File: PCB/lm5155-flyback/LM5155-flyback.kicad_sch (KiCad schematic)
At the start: 24 parts, among them Q1 Q_NMOS_DGS, T1 EP7-5801_750315825, U1 LM5155

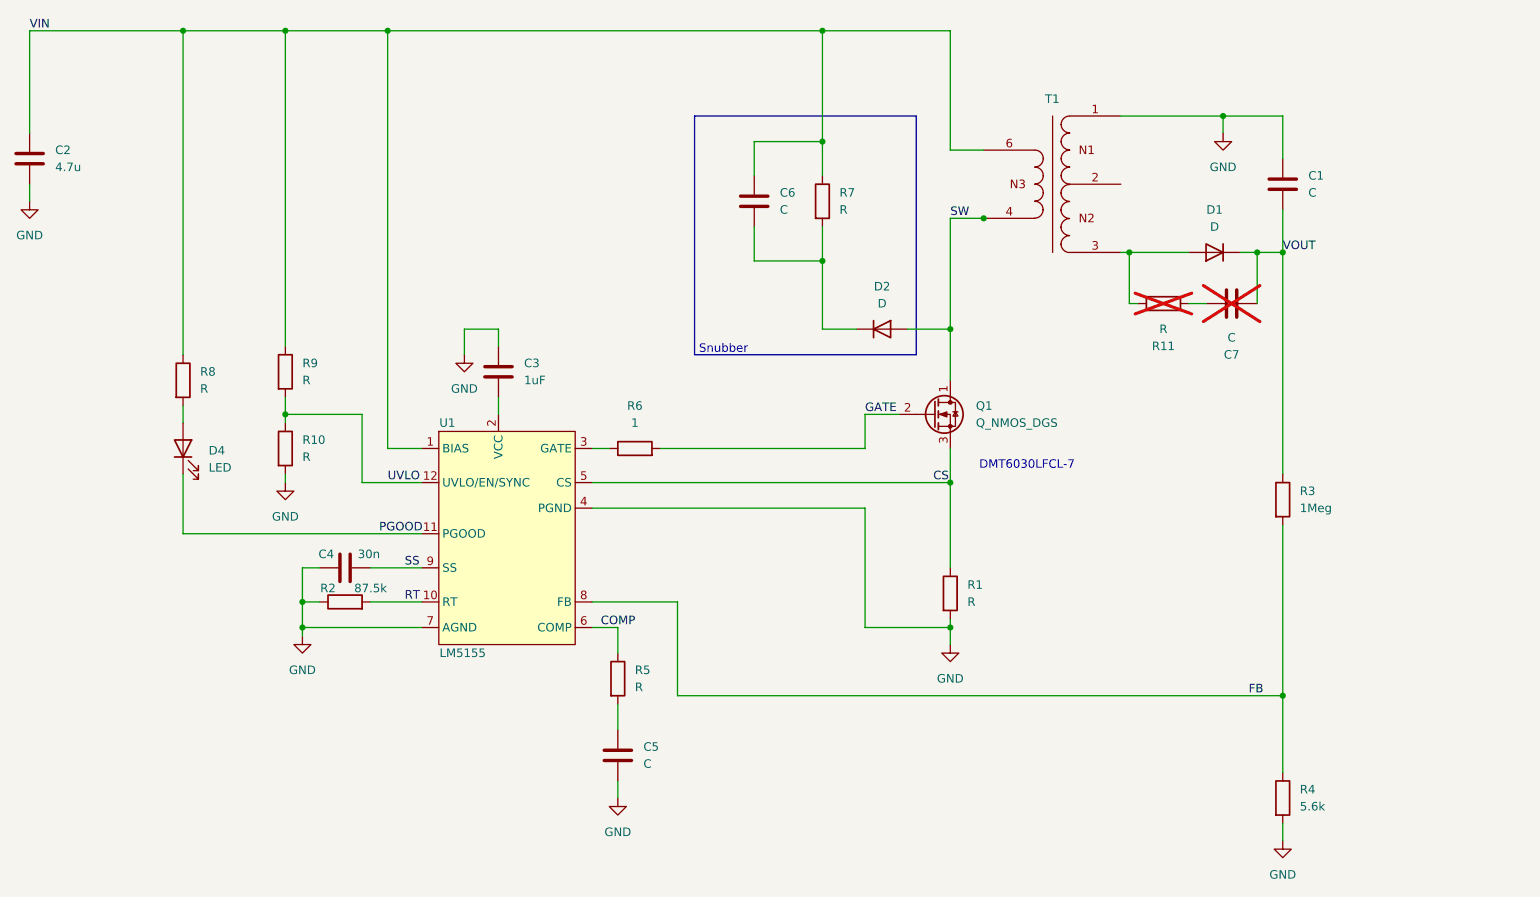
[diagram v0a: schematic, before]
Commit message: Started flyback layout and tweak simulations
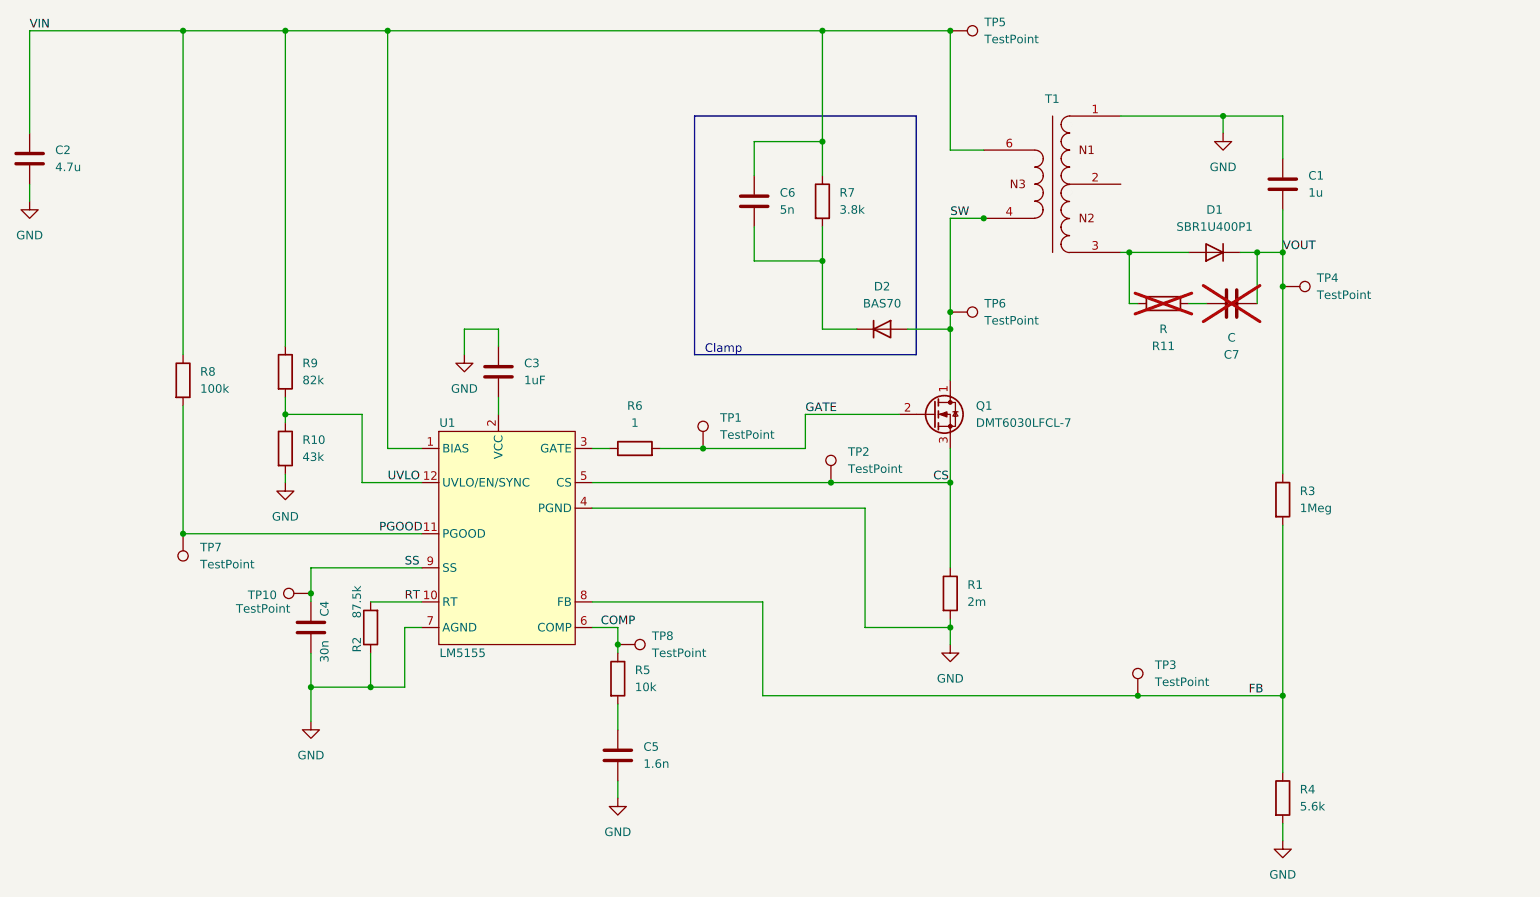
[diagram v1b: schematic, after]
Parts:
- removed D2: D, symbol Device:D
- removed D4: LED, symbol Device:LED
- added D2: BAS70, Package_TO_SOT_SMD:SOT-23, symbol LM5155-flyback:BAS70
- added TP1, TP10, TP2, TP3, TP4, TP5, TP6, TP7, TP8: TestPoint, TestPoint:TestPoint_Keystone_5019_Miniature, symbol Connector:TestPoint
- C1: value C -> 1u; footprint (none) -> Capacitor_SMD:C_2220_5750Metric_Pad1.97x5.40mm_HandSolder
- C2, C3, C4, C7: footprint (none) -> Capacitor_SMD:C_0805_2012Metric_Pad1.18x1.45mm_HandSolder
- C5: value C -> 1.6n; footprint (none) -> Capacitor_SMD:C_0805_2012Metric_Pad1.18x1.45mm_HandSolder
- C6: value C -> 5n; footprint (none) -> Capacitor_SMD:C_0805_2012Metric_Pad1.18x1.45mm_HandSolder
- D1: value D -> SBR1U400P1; footprint (none) -> Diode_SMD:D_PowerDI-123
- Q1: value Q_NMOS_DGS -> DMT6030LFCL-7; footprint (none) -> LM5155-flyback:U-DFN1616-6
- R1: value R -> 2m; footprint (none) -> Resistor_SMD:R_0805_2012Metric_Pad1.20x1.40mm_HandSolder
- R10: value R -> 43k; footprint (none) -> Resistor_SMD:R_0805_2012Metric_Pad1.20x1.40mm_HandSolder
- R11, R2, R3, R4, R6: footprint (none) -> Resistor_SMD:R_0805_2012Metric_Pad1.20x1.40mm_HandSolder
- R5: value R -> 10k; footprint (none) -> Resistor_SMD:R_0805_2012Metric_Pad1.20x1.40mm_HandSolder
- R7: value R -> 3.8k; footprint (none) -> Resistor_SMD:R_0805_2012Metric_Pad1.20x1.40mm_HandSolder
- R8: value R -> 100k; footprint (none) -> Resistor_SMD:R_0805_2012Metric_Pad1.20x1.40mm_HandSolder
- R9: value R -> 82k; footprint (none) -> Resistor_SMD:R_0805_2012Metric_Pad1.20x1.40mm_HandSolder
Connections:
- net COMP: now also TP8.1
- net CS: now also TP2.1
- net FB: now also TP3.1
- net GATE: now also TP1.1
- net GND: now also C4.2; no longer C4.1
- net PGOOD: now also R8.2, TP7.1
- net SS: now also C4.1, TP10.1; no longer C4.2
- net SW: now also D2.1 (A), TP6.1
- net VIN: now also TP5.1
- net VOUT: now also TP4.1
- net at C6.2, R7.2: now also D2.3 (K)
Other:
- note added: "Clamp"
- note removed: "DMT6030LFCL-7"
- note removed: "Snubber"
- moved on the sheet: C4, R2

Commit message: More flyback layout. Almost done!
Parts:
- removed TP10, TP7: TestPoint, TestPoint:TestPoint_Keystone_5019_Miniature, symbol Connector:TestPoint
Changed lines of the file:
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@@
 	)
 	(junction
-		(at 66.04 115.57)
-		(diameter 0)
-		(color 0 0 0 0)
-	)
-	(junction
 		(at 74.93 129.54)
 		(diameter 0)
@@
 		(color 0 0 0 0)
 	)
-	(junction
-		(at 46.99 106.68)
-		(diameter 0)
-		(color 0 0 0 0)
-	)
 	(wire
 		(pts
@@
 	(wire
 		(pts
-			(xy 66.04 115.57) (xy 66.04 116.84)
+			(xy 66.04 111.76) (xy 66.04 116.84)
 		)
 		(stroke
@@
 	(wire
 		(pts
-			(xy 66.04 111.76) (xy 66.04 115.57)
-		)
-		(stroke
-			(width 0)
-			(type default)
-		)
-	)
-	(wire
-		(pts
 			(xy 111.76 123.19) (xy 111.76 124.46)
 		)
@@
 	)
 	(symbol
-		(lib_id "Connector:TestPoint")
-		(at 46.99 106.68 180)
-		(unit 1)
-		(exclude_from_sim no)
-		(in_bom yes)
-		(on_board yes)
-		(dnp no)
-		(fields_autoplaced yes)
-		(property "Reference" "TP7"
-			(at 49.53 108.7119 0)
-			(effects
-				(font
-					(size 1.27 1.27)
-				)
-				(justify right)
-			)
-		)
-		(property "Value" "TestPoint"
-			(at 49.53 111.2519 0)
-			(effects
-				(font
-					(size 1.27 1.27)
-				)
-				(justify right)
-			)
-		)
-		(property "Footprint" "TestPoint:TestPoint_Keystone_5019_Miniature"
-			(at 41.91 106.68 0)
-			(effects
-				(font
-					(size 1.27 1.27)
-				)
-				(hide yes)
-			)
-		)
-		(property "Datasheet" "~"
-			(at 41.91 106.68 0)
-			(effects
-				(font
-					(size 1.27 1.27)
-				)
-				(hide yes)
-			)
-		)
-		(property "Description" "test point"
-			(at 46.99 106.68 0)
-			(effects
-				(font
-					(size 1.27 1.27)
-				)
-				(hide yes)
-			)
-		)
-		(pin "1"
-		)
-		(instances
-			(project "LM5155-flyback"
-				(path "/75d4b288-a1f8-4f29-bb2f-aeffb4f40ccc"
-					(reference "TP7")
-					(unit 1)
-				)
-			)
-		)
-	)
-	(symbol
 		(lib_id "Device:R")
 		(at 74.93 120.65 180)
@@
 					(unit 1)
 				)
-			)
-		)
-	)
-	(symbol
-		(lib_id "Connector:TestPoint")
-		(at 66.04 115.57 90)
-		(mirror x)
-		(unit 1)
-		(exclude_from_sim no)
-		(in_bom yes)
-		(on_board yes)
-		(dnp no)
-		(property "Reference" "TP10"
-			(at 56.642 115.824 90)
-			(effects
-				(font
-					(size 1.27 1.27)
-				)
-				(justify right)
-			)
-		)
-		(property "Value" "TestPoint"
-			(at 54.864 117.856 90)
-			(effects
-				(font
-					(size 1.27 1.27)
-				)
-				(justify right)
-			)
-		)
-		(property "Footprint" "TestPoint:TestPoint_Keystone_5019_Miniature"
-			(at 66.04 120.65 0)
-			(effects
-				(font
-					(size 1.27 1.27)
-				)
-				(hide yes)
-			)
-		)
-		(property "Datasheet" "~"
-			(at 66.04 120.65 0)
-			(effects
-				(font
-					(size 1.27 1.27)
-				)
-				(hide yes)
-			)
-		)
-		(property "Description" "test point"
-			(at 66.04 115.57 0)
-			(effects
-				(font
-					(size 1.27 1.27)
-				)
-				(hide yes)
-			)
-		)
-		(pin "1"
-		)
-		(instances
-			(project "LM5155-flyback"
-				(path "/75d4b288-a1f8-4f29-bb2f-aeffb4f40ccc"
-					(reference "TP10")
-					(unit 1)
-				)

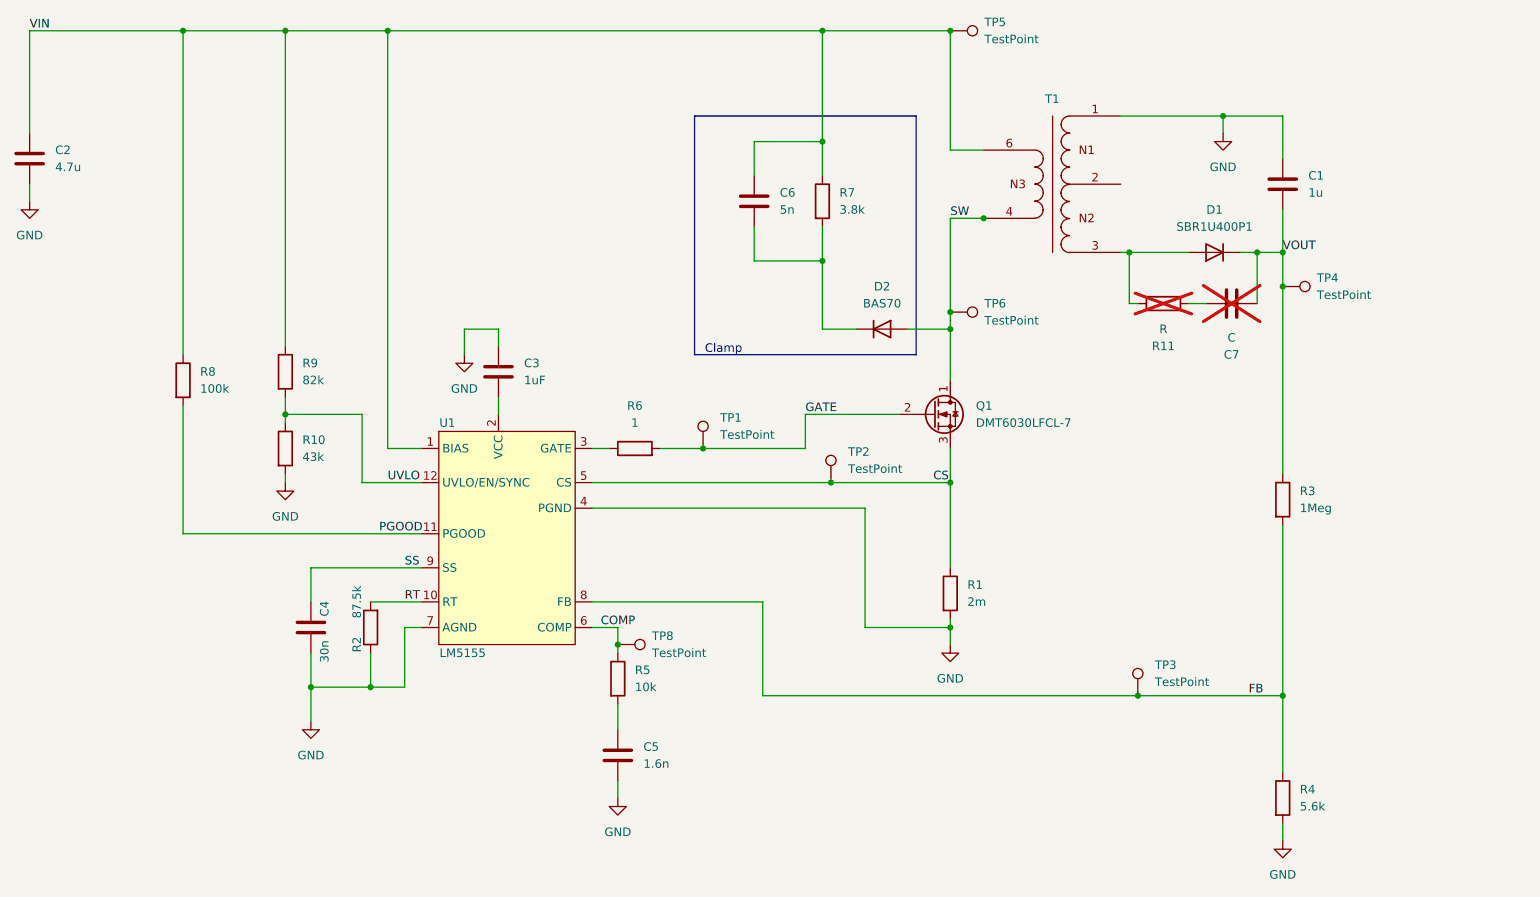
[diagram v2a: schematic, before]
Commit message: Fix small issue with feedback resistors. Hopefully wont cause real issues with Rev 1
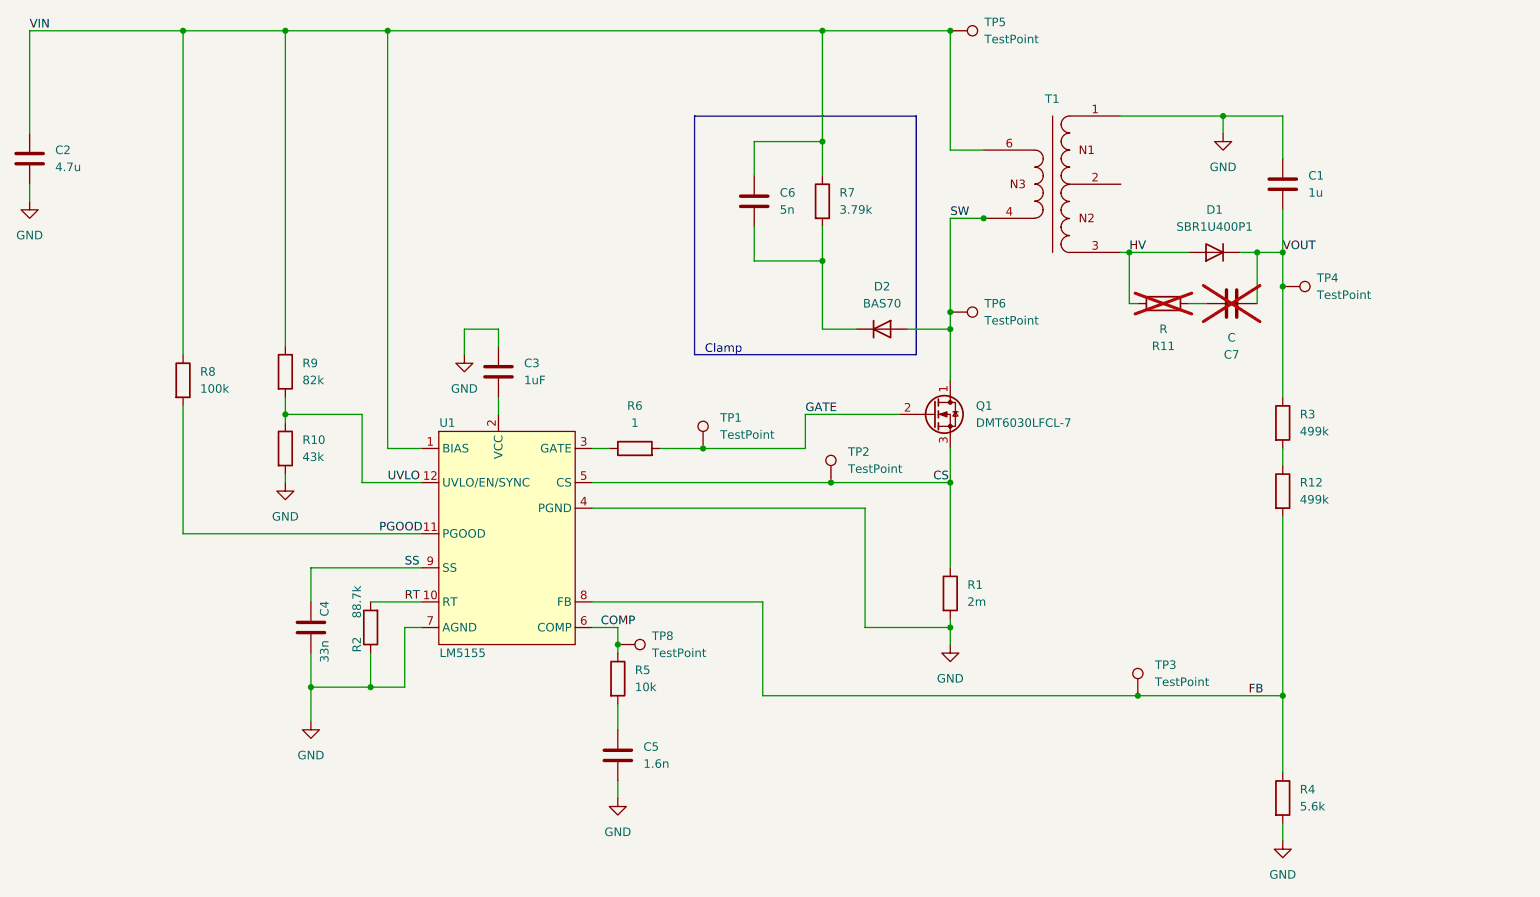
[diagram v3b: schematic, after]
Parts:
- added R12: 499k, Resistor_SMD:R_0805_2012Metric_Pad1.20x1.40mm_HandSolder, symbol Device:R
- C4: value 30n -> 33n
- R2: value 87.5k -> 88.7k
- R3: value 1Meg -> 499k
- R7: value 3.8k -> 3.79k
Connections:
- net FB: now also R12.2; no longer R3.2
- net HV: now reaches D1.2 (A), R11.1, T1.3
- new net: R12.1, R3.2
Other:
- company: (none) -> bartlettD
- title: (none) -> LM5155 Nixie Flyback
- moved on the sheet: R3
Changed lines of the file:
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@@
 	(generator_version "9.0")
 	(paper "A4")
+	(title_block
+		(title "LM5155 Nixie Flyback")
+		(date "2026-02-03")
+		(rev "2")
+		(company "bartlettD")
+	)
 	(rectangle
 		(start 123.19 44.45)
@@
 	)
 	(junction
-		(at 210.82 130.81)
+		(at 210.82 69.85)
 		(diameter 0)
 		(color 0 0 0 0)
 	)
 	(junction
-		(at 210.82 69.85)
+		(at 210.82 130.81)
 		(diameter 0)
 		(color 0 0 0 0)
@@
 	(wire
 		(pts
+			(xy 210.82 93.98) (xy 210.82 96.52)
+		)
+		(stroke
+			(width 0)
+			(type default)
+		)
+	)
+	(wire
+		(pts
 			(xy 74.93 116.84) (xy 82.55 116.84)
 		)
@@
 	(wire
 		(pts
-			(xy 210.82 69.85) (xy 210.82 97.79)
+			(xy 210.82 69.85) (xy 210.82 86.36)
 		)
 		(stroke
@@
 	(wire
 		(pts
+			(xy 210.82 104.14) (xy 210.82 130.81)
+		)
+		(stroke
+			(width 0)
+			(type default)
+		)
+	)
+	(wire
+		(pts
 			(xy 107.95 116.84) (xy 133.35 116.84)
 		)
@@
 	(wire
 		(pts
-			(xy 210.82 105.41) (xy 210.82 130.81)
-		)
-		(stroke
-			(width 0)
-			(type default)
-		)
-	)
-	(wire
-		(pts
 			(xy 148.59 120.65) (xy 161.29 120.65)
 		)
@@
 		)
 	)
+	(label "HV"
+		(at 187.96 64.77 0)
+		(effects
+			(font
+				(size 1.27 1.27)
+			)
+			(justify left bottom)
+		)
+	)
 	(label "CS"
 		(at 158.75 99.06 0)
@@
 			)
 		)
-		(property "Value" "87.5k"
+		(property "Value" "88.7k"
 			(at 72.898 116.84 90)
 			(effects
@@
 			)
 		)
-		(property "Value" "30n"
+		(property "Value" "33n"
 			(at 68.072 124.206 90)
 			(effects
@@
 	)
 	(symbol
+		(lib_id "Device:R")
+		(at 210.82 100.33 0)
+		(unit 1)
+		(exclude_from_sim no)
+		(in_bom yes)
+		(on_board yes)
+		(dnp no)
+		(fields_autoplaced yes)
+		(property "Reference" "R12"
+			(at 213.36 99.0599 0)
+			(effects
+				(font
+					(size 1.27 1.27)
+				)
+				(justify left)
+			)
+		)
+		(property "Value" "499k"
+			(at 213.36 101.5999 0)
+			(effects
+				(font
+					(size 1.27 1.27)
+				)
+				(justify left)
+			)
+		)
+		(property "Footprint" "Resistor_SMD:R_0805_2012Metric_Pad1.20x1.40mm_HandSolder"
+			(at 209.042 100.33 90)
+			(effects
+				(font
+					(size 1.27 1.27)
+				)
+				(hide yes)
+			)
+		)
+		(property "Datasheet" "~"
+			(at 210.82 100.33 0)
+			(effects
+				(font
+					(size 1.27 1.27)
+				)
+				(hide yes)
+			)
+		)
+		(property "Description" "Resistor"
+			(at 210.82 100.33 0)
+			(effects
+				(font
+					(size 1.27 1.27)
+				)
+				(hide yes)
+			)
+		)
+		(pin "2"
+		)
+		(pin "1"
+		)
+		(instances
+			(project "LM5155-flyback"
+				(path "/75d4b288-a1f8-4f29-bb2f-aeffb4f40ccc"
+					(reference "R12")
+					(unit 1)
+				)
+			)
+		)
+	)
+	(symbol
 		(lib_id "power:GND")
 		(at 201.93 46.99 0)
@@
 	(symbol
 		(lib_id "Device:R")
-		(at 210.82 101.6 0)
+		(at 210.82 90.17 0)
 		(unit 1)
 		(exclude_from_sim no)
@@
 		(fields_autoplaced yes)
 		(property "Reference" "R3"
-			(at 213.36 100.3299 0)
+			(at 213.36 88.8999 0)
 			(effects
 				(font
@@
 			)
 		)
-		(property "Value" "1Meg"
-			(at 213.36 102.8699 0)
+		(property "Value" "499k"
+			(at 213.36 91.4399 0)
 			(effects
 				(font
@@
 		)
 		(property "Footprint" "Resistor_SMD:R_0805_2012Metric_Pad1.20x1.40mm_HandSolder"
-			(at 209.042 101.6 90)
+			(at 209.042 90.17 90)
 			(effects
 				(font
@@
 		)
 		(property "Datasheet" "~"
-			(at 210.82 101.6 0)
+			(at 210.82 90.17 0)
 			(effects
 				(font
@@
 		)
 		(property "Description" "Resistor"
-			(at 210.82 101.6 0)
+			(at 210.82 90.17 0)
 			(effects
 				(font
@@
 			)
 		)
-		(property "Value" "3.8k"
+		(property "Value" "3.79k"
 			(at 144.78 58.4199 0)
 			(effects
